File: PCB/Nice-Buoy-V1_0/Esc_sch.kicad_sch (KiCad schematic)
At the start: 4 parts, among them J401 ESC-BB, J402 ESC-SB

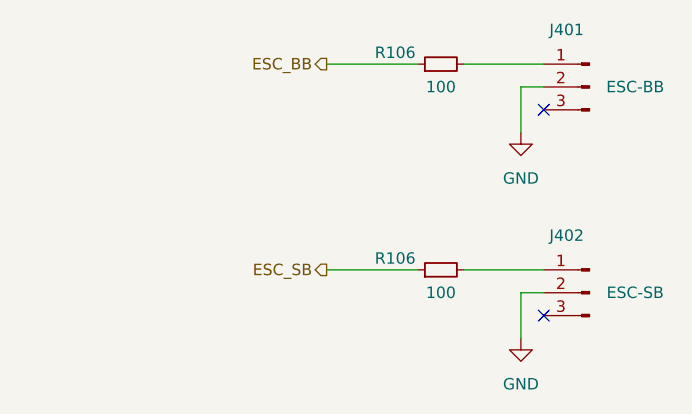
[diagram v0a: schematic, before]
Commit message: Buzzer added key readoud improved
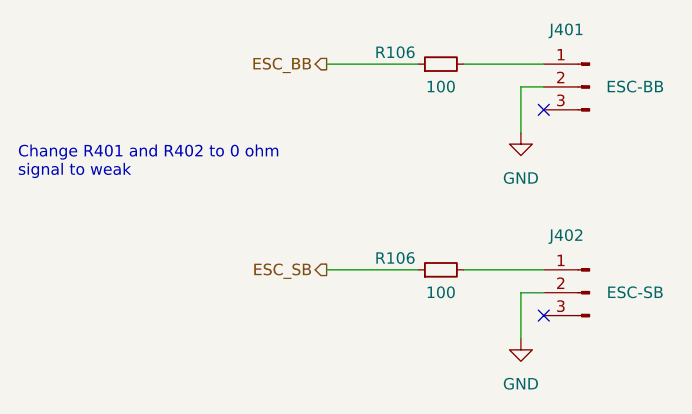
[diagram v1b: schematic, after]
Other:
- note added: "Change R401 and R402 to 0 ohm signal to weak"
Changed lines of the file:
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@@
     (stroke (width 0) (type default))
+  )
+  (text "Change R401 and R402 to 0 ohm\nsignal to weak" (at 72.39 95.25 0)
+    (effects (font (size 1.27 1.27)) (justify left bottom))
   )
   (hierarchical_label "ESC_BB" (shape output) (at 106.68 82.55 180) (fields_autoplaced)

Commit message: dingus
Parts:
- renumbered R106 to R401, R106 to R402
